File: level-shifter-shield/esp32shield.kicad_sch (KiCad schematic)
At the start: 40 parts, among them J1 Power_Terminal, J10 Screw_Terminal_01x02, J11 Screw_Terminal_01x02, J2 Conn_01x19_Pin, J3 Power_Terminal, J4 Conn_01x19_Socket, J5 Power_Terminal, J6 Conn_01x19_Socket, J7 Conn_01x19_Pin, J8 Screw_Terminal_01x02, J9 Screw_Terminal_01x02, U1 LM7805, U2 IXDD604PI, U3 IXDD604PI, U4 IXDD604PI, U5 IXDD604PI

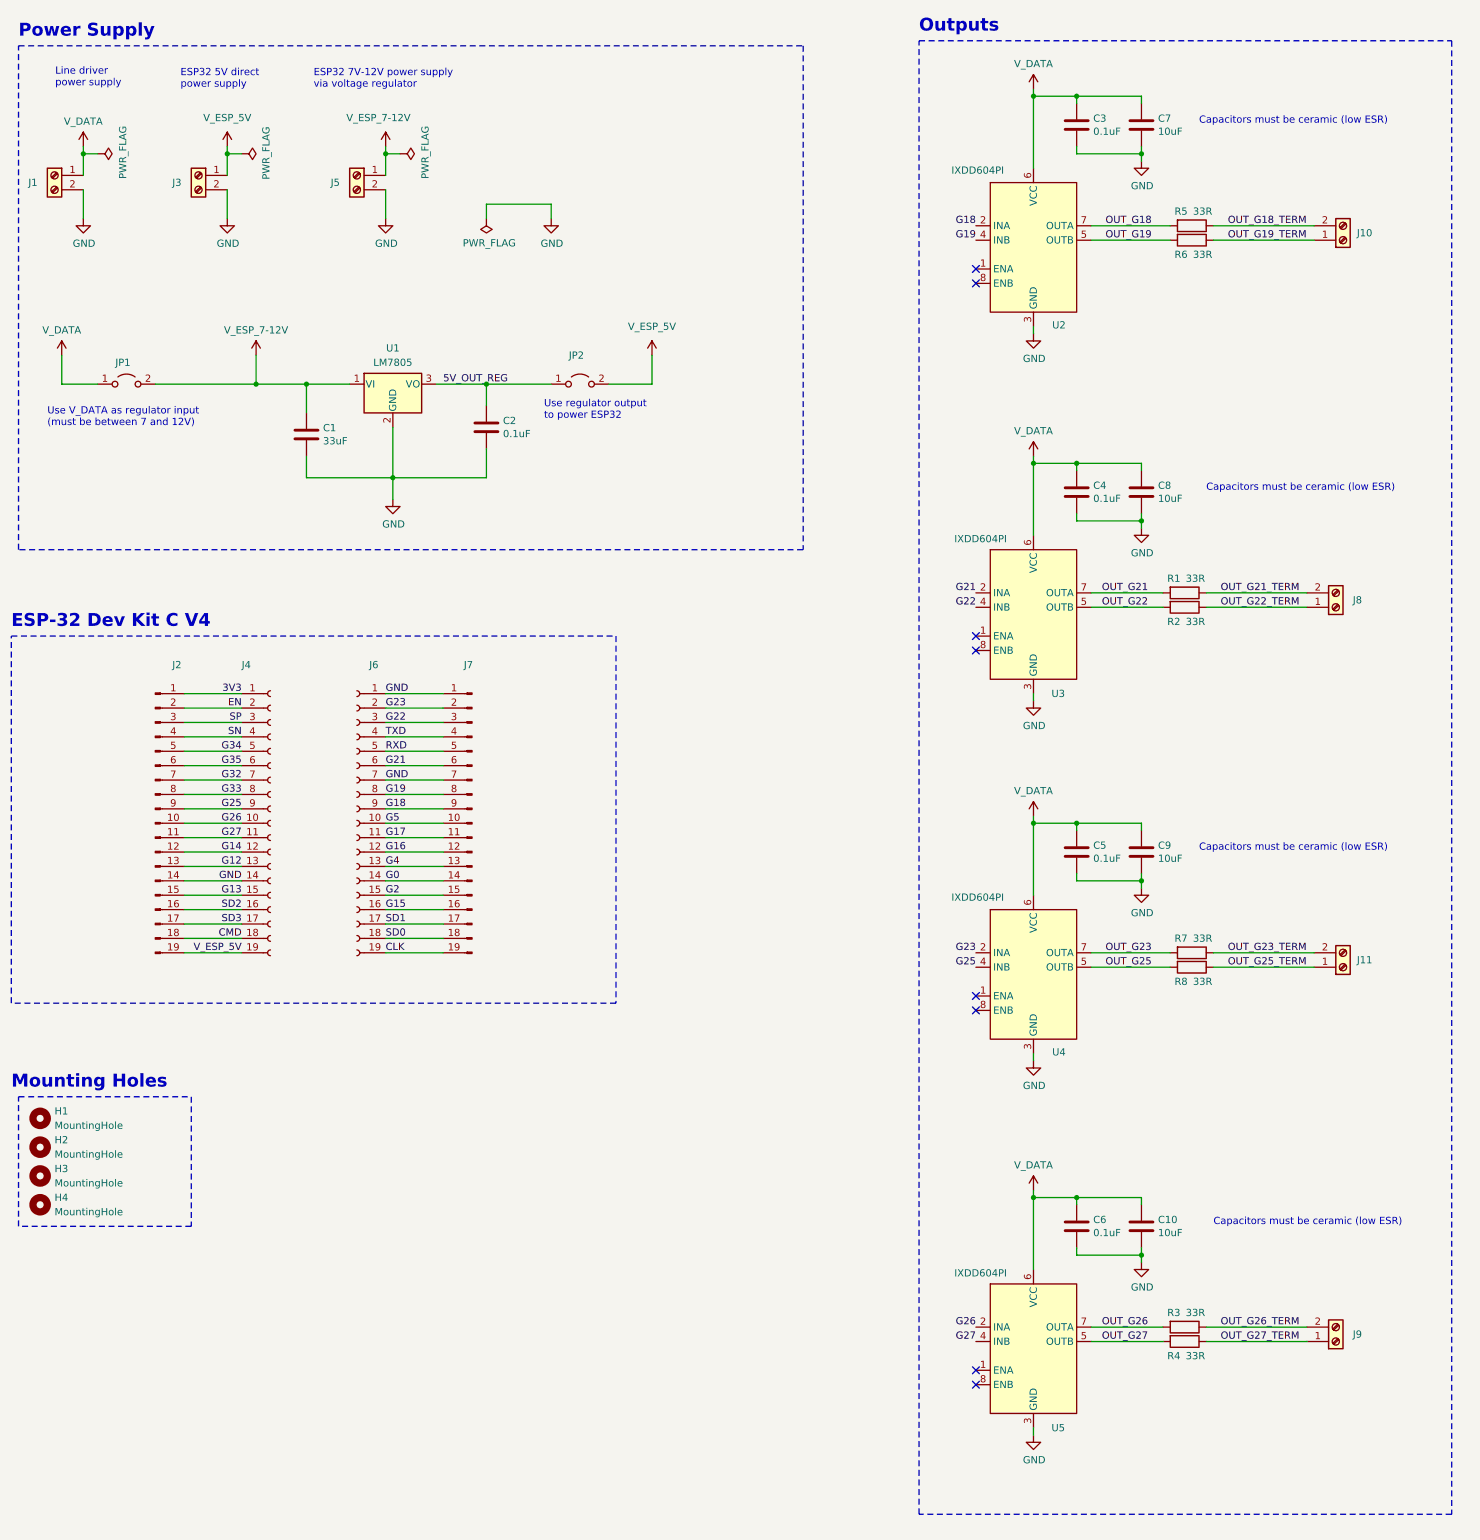
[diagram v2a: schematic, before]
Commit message: Adapt level shifter shield layout and add routing
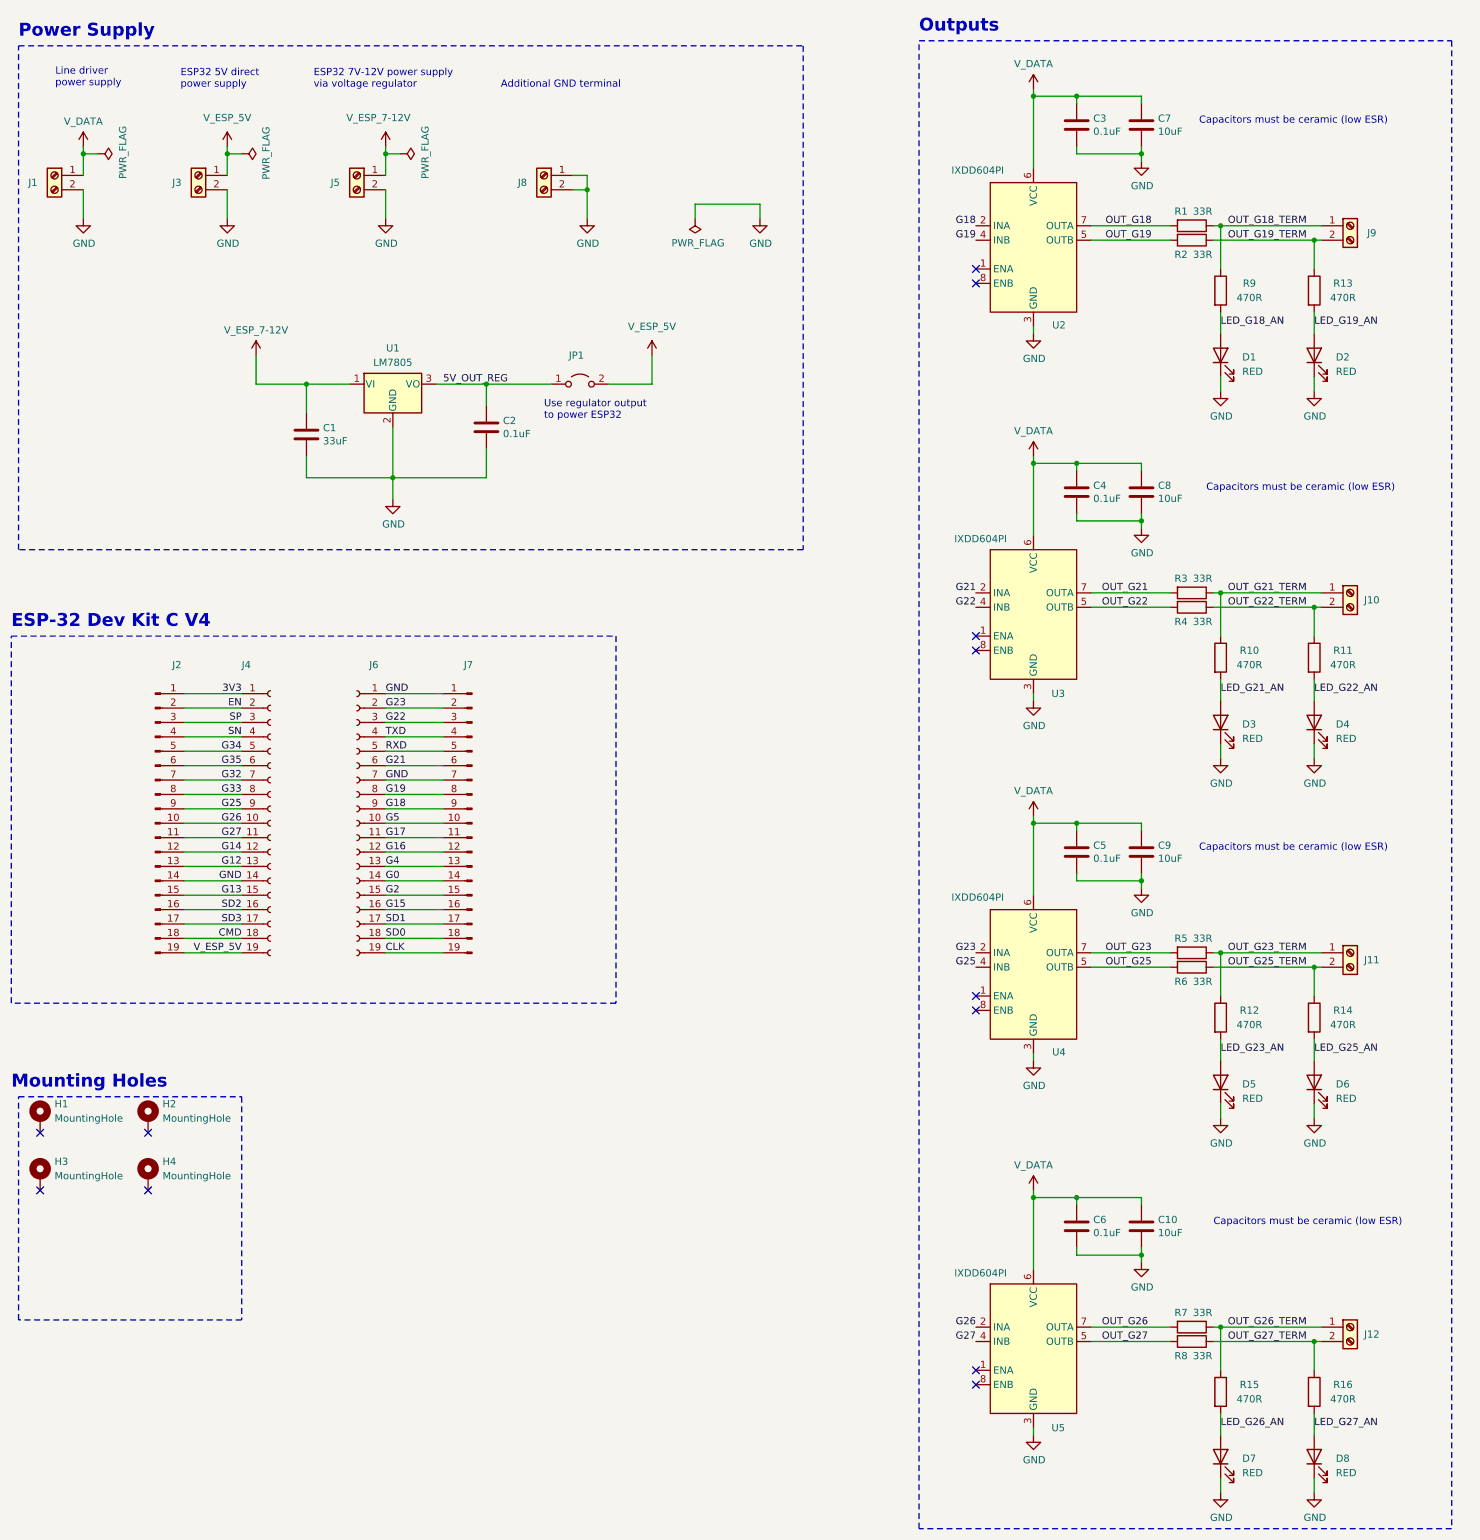
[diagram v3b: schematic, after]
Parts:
- removed JP1: Jumper_2_Open, Connector_PinHeader_2.54mm:PinHeader_1x02_P2.54mm_Vertical, symbol Jumper:Jumper_2_Open
- added D1, D2, D3, D4, D5, D6, D7, D8: RED, LED_THT:LED_D3.0mm, symbol Device:LED
- added J8: Power_Terminal, TerminalBlock_Phoenix:TerminalBlock_Phoenix_MKDS-1,5-2-5.08_1x02_P5.08mm_Horizontal, symbol Connector:Screw_Terminal_01x02
- added R10, R11, R12, R13, R14, R15, R16, R9: 470R, Resistor_THT:R_Axial_DIN0207_L6.3mm_D2.5mm_P2.54mm_Vertical, symbol Device:R
- C1, C10, C7, C8, C9: footprint Capacitor_THT:C_Disc_D3.0mm_W1.6mm_P2.50mm -> Capacitor_THT:C_Disc_D4.7mm_W2.5mm_P5.00mm
- H1, H2, H3, H4: footprint MountingHole:MountingHole_2.2mm_M2 -> MountingHole:MountingHole_2.2mm_M2_Pad; symbol Mechanical:MountingHole -> Mechanical:MountingHole_Pad
- renumbered J8 to J10, J9 to J12, J10 to J9, JP2 to JP1, R5 to R1, R6 to R2, R1 to R3, R2 to R4, R7 to R5, R8 to R6, R3 to R7, R4 to R8
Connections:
- net GND: now also D1.1 (K), D2.1 (K), D3.1 (K), D4.1 (K), D5.1 (K), D6.1 (K), D7.1 (K), D8.1 (K), J8.1 (Pin_1), J8.2 (Pin_2)
- net OUT_G18_TERM: now also J9.1 (Pin_1), R9.1; no longer J9.2 (Pin_2)
- net OUT_G19_TERM: now also J9.2 (Pin_2), R13.1; no longer J9.1 (Pin_1)
- net OUT_G21_TERM: now also J10.1 (Pin_1), R10.1; no longer J10.2 (Pin_2)
- net OUT_G22_TERM: now also J10.2 (Pin_2), R11.1; no longer J10.1 (Pin_1)
- net OUT_G23_TERM: now also J11.1 (Pin_1), R12.1; no longer J11.2 (Pin_2)
- net OUT_G25_TERM: now also J11.2 (Pin_2), R14.1; no longer J11.1 (Pin_1)
- net OUT_G26_TERM: now also J12.1 (Pin_1), R15.1; no longer J12.2 (Pin_2)
- net OUT_G27_TERM: now also J12.2 (Pin_2), R16.1; no longer J12.1 (Pin_1)
- new net LED_G18_AN: D1.2 (A), R9.2
- new net LED_G19_AN: D2.2 (A), R13.2
- new net LED_G21_AN: D3.2 (A), R10.2
- new net LED_G22_AN: D4.2 (A), R11.2
- new net LED_G23_AN: D5.2 (A), R12.2
- new net LED_G25_AN: D6.2 (A), R14.2
- new net LED_G26_AN: D7.2 (A), R15.2
- new net LED_G27_AN: D8.2 (A), R16.2
- no-connect marks 8 -> 12
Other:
- note added: "Additional GND terminal"
- note removed: "Use V_DATA as regulator input (must be between 7 and 12V)"
- moved on the sheet: J10, J11, J12, J9, R3, R4, R7, R8

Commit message: Add production files for level shifter shield
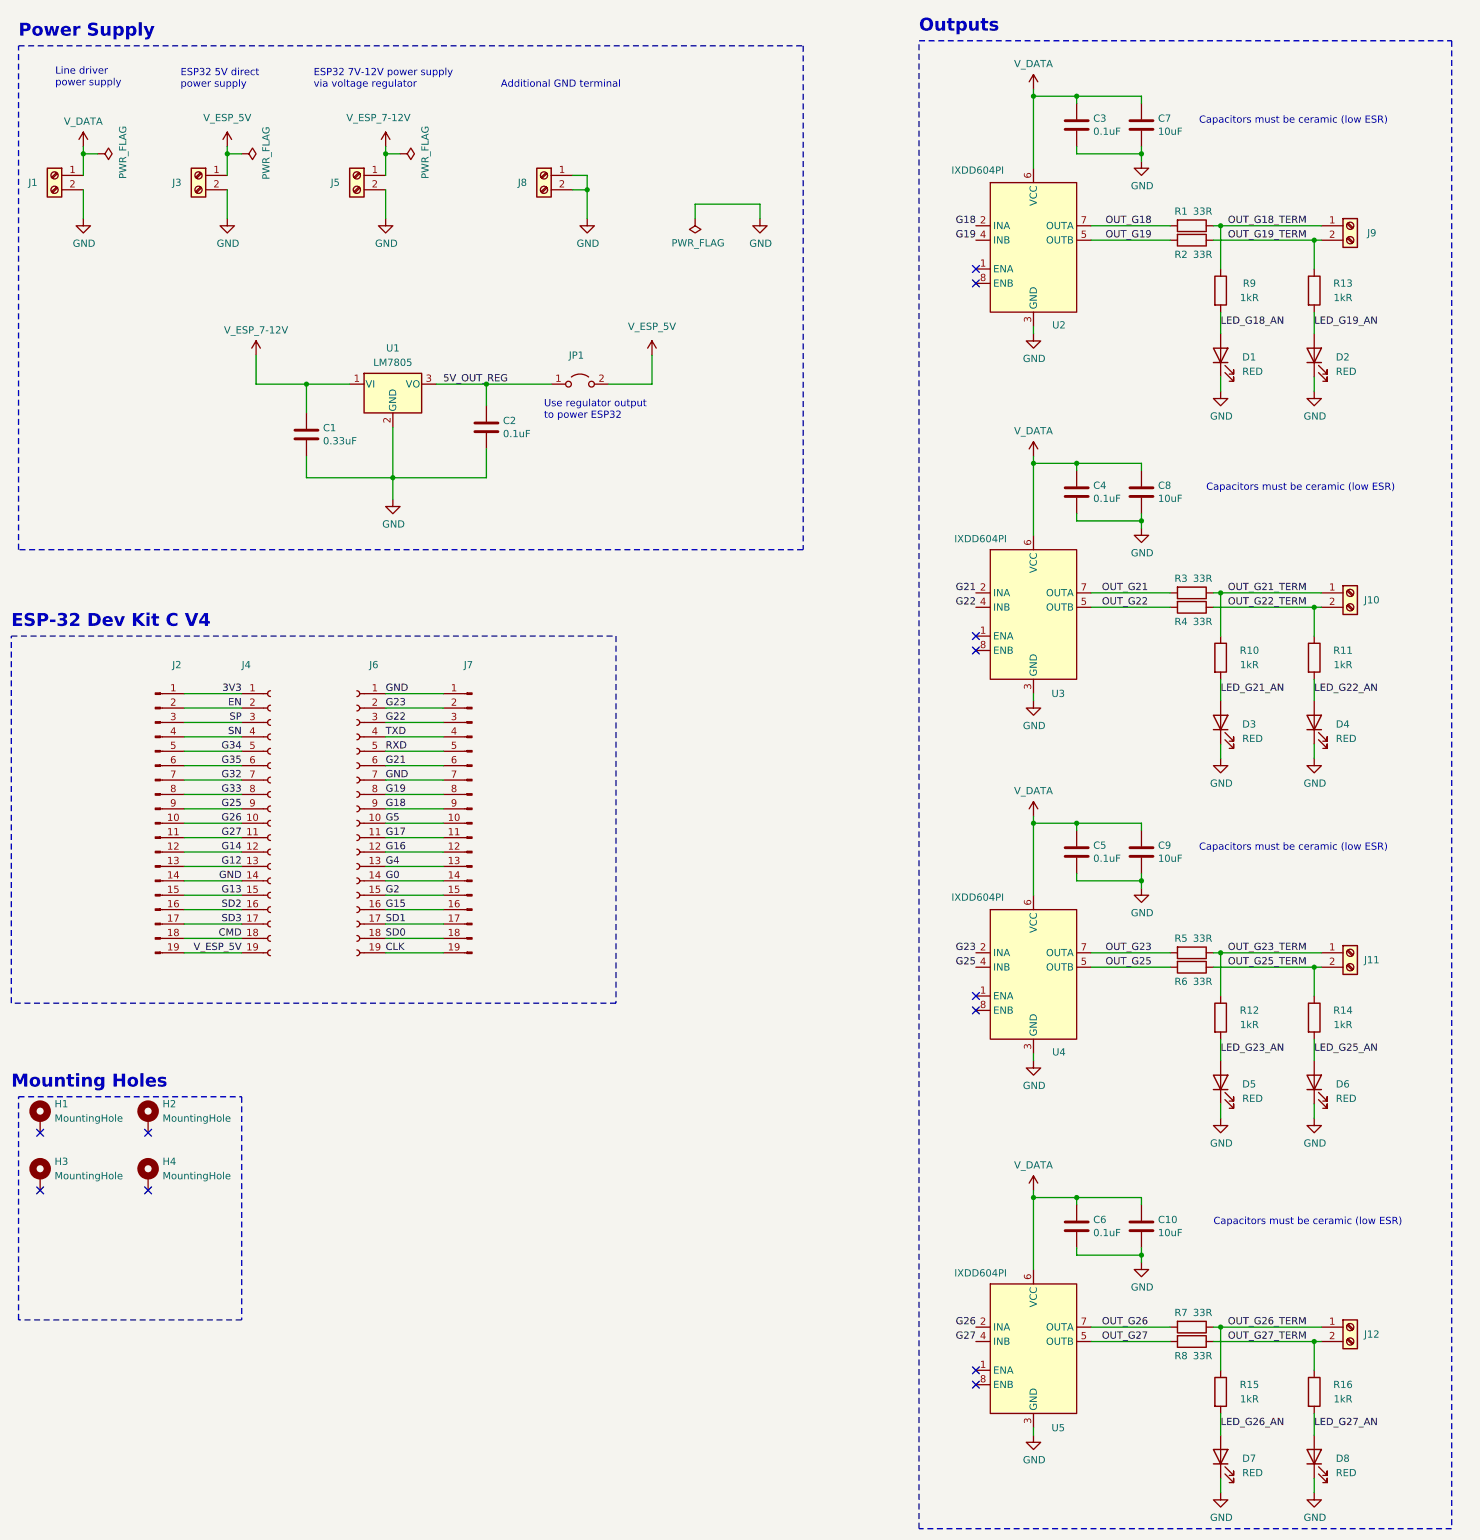
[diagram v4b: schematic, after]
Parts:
- C1: value 33uF -> 0.33uF; footprint Capacitor_THT:C_Disc_D4.7mm_W2.5mm_P5.00mm -> Capacitor_THT:C_Disc_D3.0mm_W1.6mm_P2.50mm
- R10, R11, R12, R13, R14, R15, R16, R9: value 470R -> 1kR
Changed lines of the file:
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@@
       (effects (font (size 1.27 1.27)) (justify left))
     )
-    (property "Value" "33uF" (at 72.771 91.313 0)
-      (effects (font (size 1.27 1.27)) (justify left))
-    )
-    (property "Footprint" "Capacitor_THT:C_Disc_D4.7mm_W2.5mm_P5.00mm" (at 70.8152 93.98 0)
+    (property "Value" "0.33uF" (at 72.771 91.313 0)
+      (effects (font (size 1.27 1.27)) (justify left))
+    )
+    (property "Footprint" "Capacitor_THT:C_Disc_D3.0mm_W1.6mm_P2.50mm" (at 70.8152 93.98 0)
       (effects (font (size 1.27 1.27)) hide)
     )
@@
       (effects (font (size 1.27 1.27)))
     )
-    (property "Value" "470R" (at 252.73 130.81 0)
+    (property "Value" "1kR" (at 252.73 130.81 0)
       (effects (font (size 1.27 1.27)))
     )
@@
       (effects (font (size 1.27 1.27)))
     )
-    (property "Value" "470R" (at 236.22 130.81 0)
+    (property "Value" "1kR" (at 236.22 130.81 0)
       (effects (font (size 1.27 1.27)))
     )
@@
       (effects (font (size 1.27 1.27)))
     )
-    (property "Value" "470R" (at 252.73 260.35 0)
+    (property "Value" "1kR" (at 252.73 260.35 0)
       (effects (font (size 1.27 1.27)))
     )
@@
       (effects (font (size 1.27 1.27)))
     )
-    (property "Value" "470R" (at 236.22 194.31 0)
+    (property "Value" "1kR" (at 236.22 194.31 0)
       (effects (font (size 1.27 1.27)))
     )
@@
       (effects (font (size 1.27 1.27)))
     )
-    (property "Value" "470R" (at 252.73 194.31 0)
+    (property "Value" "1kR" (at 252.73 194.31 0)
       (effects (font (size 1.27 1.27)))
     )
@@
       (effects (font (size 1.27 1.27)))
     )
-    (property "Value" "470R" (at 252.73 66.04 0)
+    (property "Value" "1kR" (at 252.73 66.04 0)
       (effects (font (size 1.27 1.27)))
     )
@@
       (effects (font (size 1.27 1.27)))
     )
-    (property "Value" "470R" (at 236.22 260.35 0)
+    (property "Value" "1kR" (at 236.22 260.35 0)
       (effects (font (size 1.27 1.27)))
     )
@@
       (effects (font (size 1.27 1.27)))
     )
-    (property "Value" "470R" (at 236.22 66.04 0)
-      (effects (font (size 1.27 1.27)))
-    )
+    (property "Value" "1kR" (at 236.22 66.04 0)
+      (effects (font (size 1.27 1.27)))
+    )
